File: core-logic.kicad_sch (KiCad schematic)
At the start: 32 parts, among them J5 TC2030-IDC, SW1 SW_Push, U1 STM32H723ZGI6, Y1 NX3215SA 32.768kHz, Y2 NX2016SA 25MHz

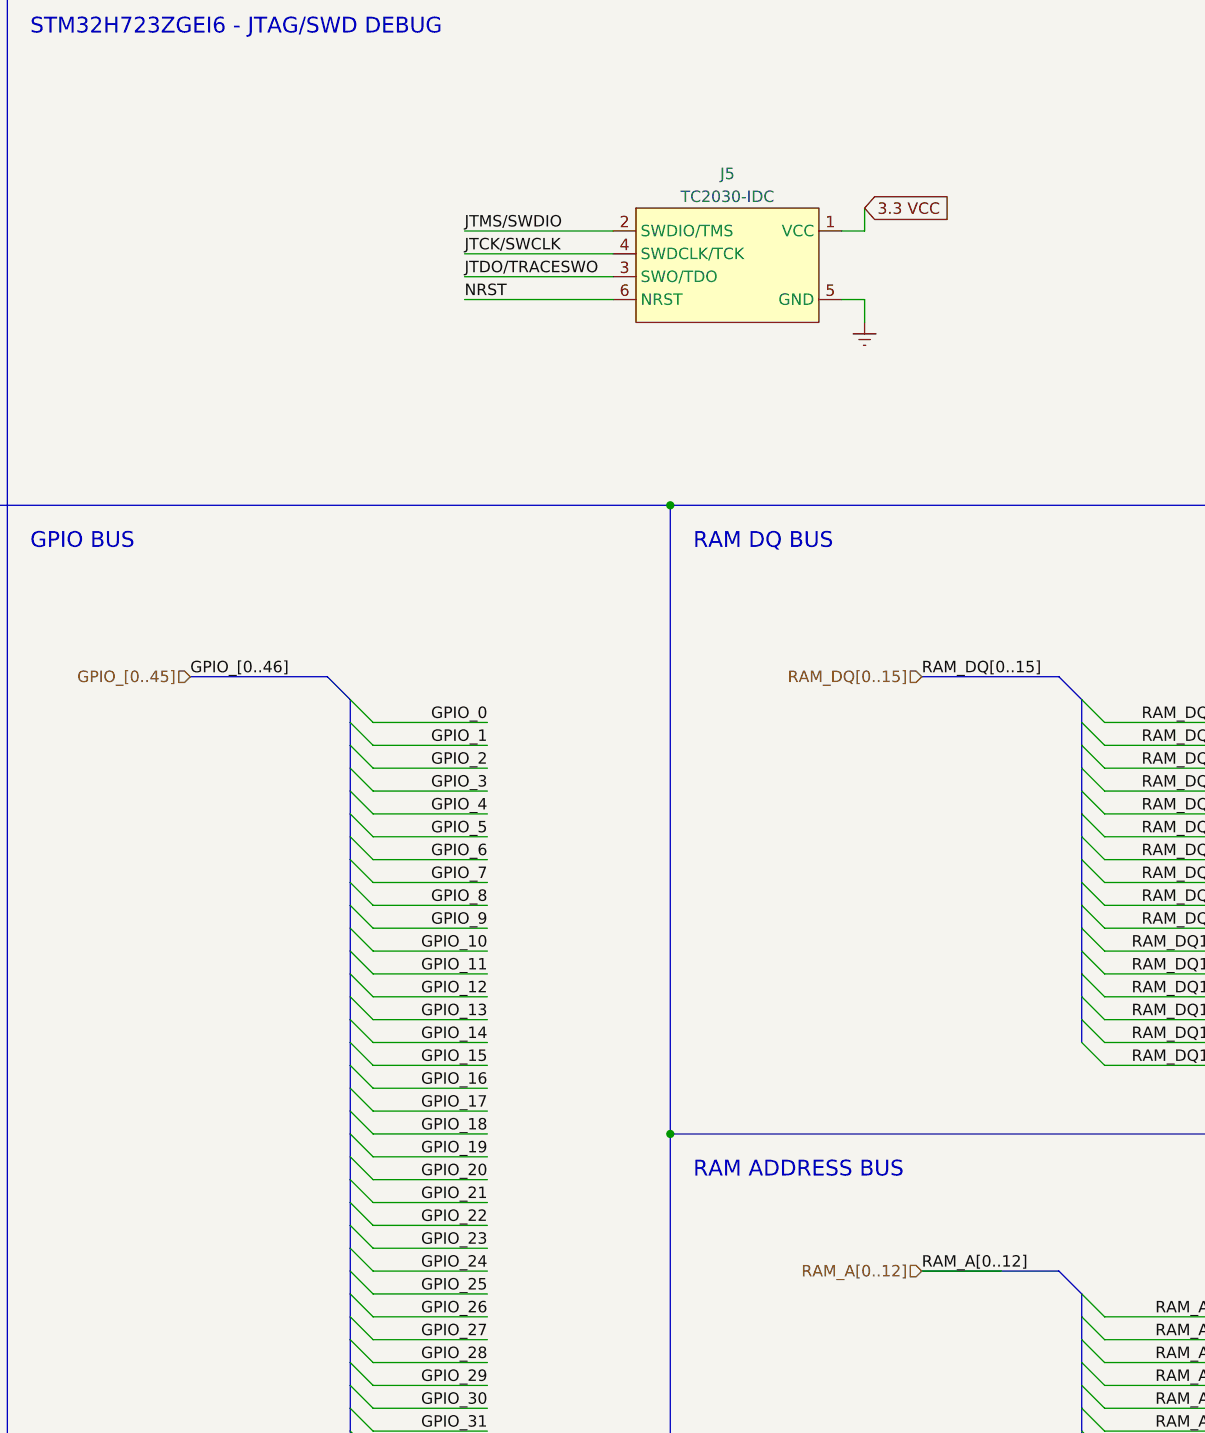
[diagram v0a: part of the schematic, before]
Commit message: updated bus aliases; added resistor values to RF section; added component to Fruitly_RF library
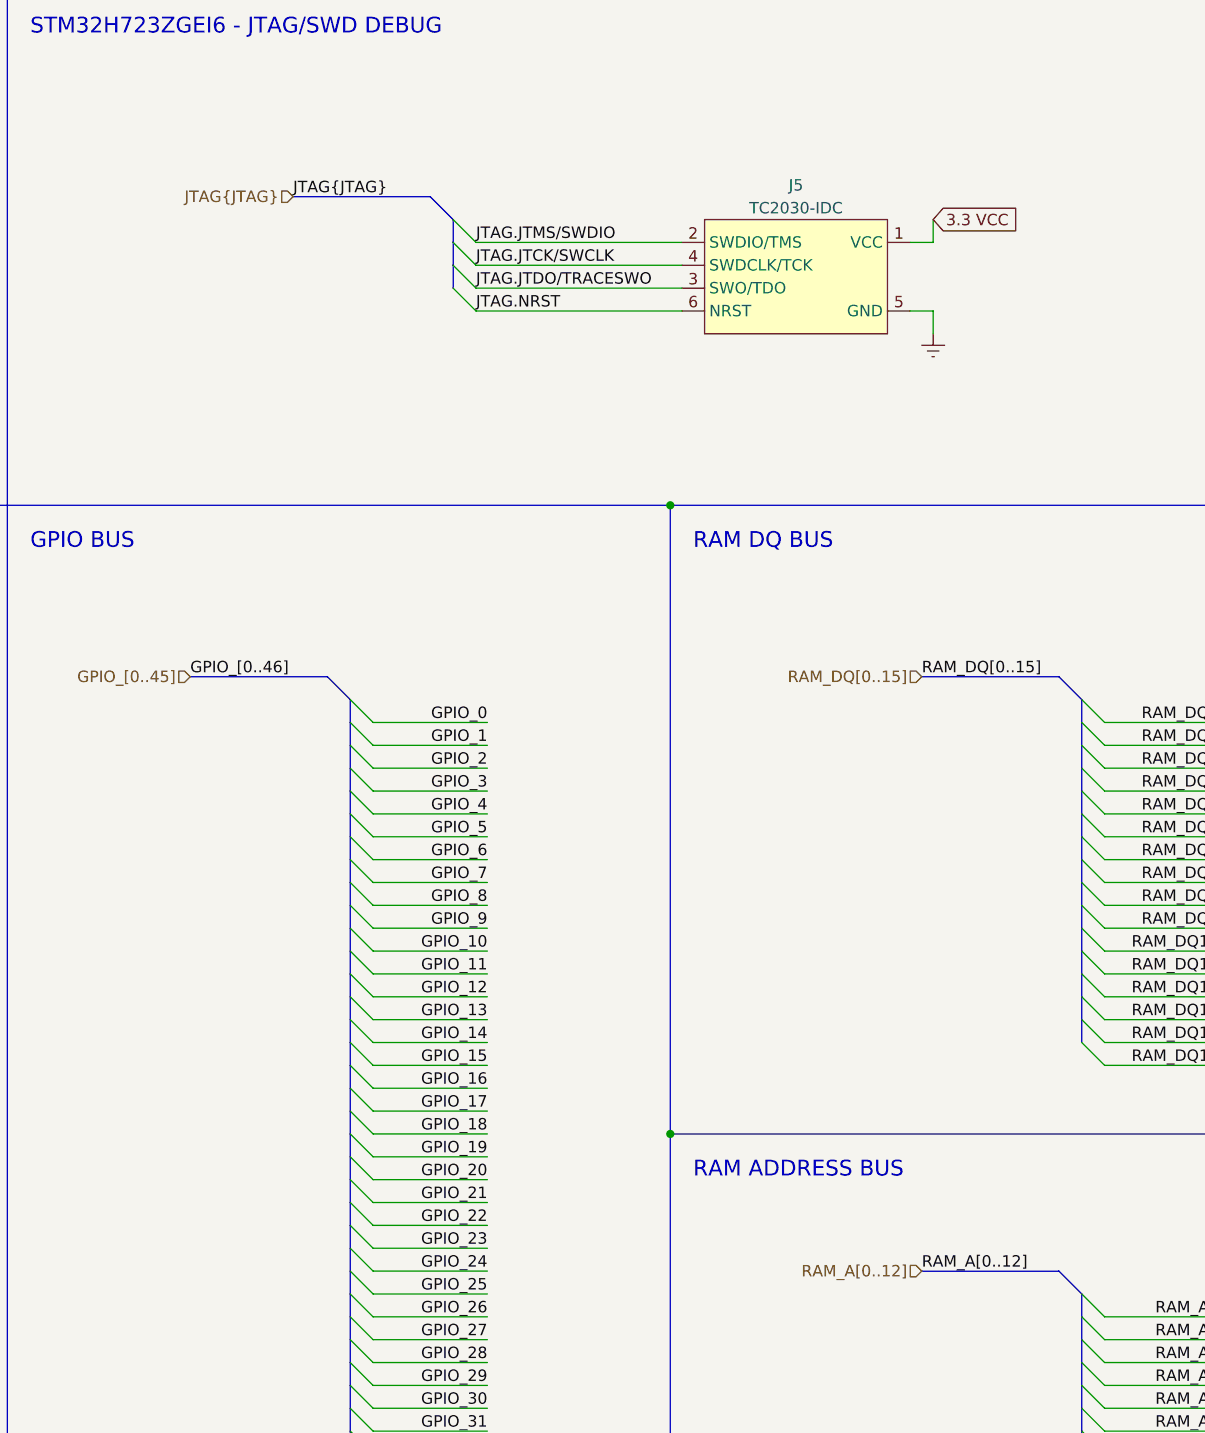
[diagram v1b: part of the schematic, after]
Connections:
- net JTCK/SWCLK: no longer J5.4 (SWDCLK/TCK)
- net JTDO/TRACESWO: no longer J5.3 (SWO/TDO)
- net JTMS/SWDIO: no longer J5.2 (SWDIO/TMS)
- net NRST: no longer J5.6 (NRST)
- new net JTAG.JTCK/SWCLK: J5.4 (SWDCLK/TCK)
- new net JTAG.JTDO/TRACESWO: J5.3 (SWO/TDO)
- new net JTAG.JTMS/SWDIO: J5.2 (SWDIO/TMS)
- new net JTAG.NRST: J5.6 (NRST)
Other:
- moved on the sheet: J5
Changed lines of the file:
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@@
     (company "Cerebral Systems Inc.")
   )
+  (bus_alias "JTAG" (members "JTMS/SWDIO" "JTCK/SWCLK" "JTDO/TRACESWO" "NRST"))
   (junction (at 113.03 232.41) (diameter 0) (color 0 0 0 0)
   )
@@
     (stroke (width 0) (type default) (color 255 153 0 1))
   )
+  (bus_entry (at 339.09 41.91) (size 2.54 2.54)
+    (stroke (width 0) (type default) (color 0 0 0 0))
+  )
   (bus_entry (at 407.67 227.33) (size 2.54 2.54)
     (stroke (width 0) (type default) (color 0 0 0 0))
@@
     (stroke (width 0) (type default) (color 255 153 0 1))
   )
+  (bus_entry (at 339.09 44.45) (size 2.54 2.54)
+    (stroke (width 0) (type default) (color 0 0 0 0))
+  )
   (bus_entry (at 408.94 189.23) (size 2.54 2.54)
     (stroke (width 0) (type default) (color 0 255 255 1))
@@
     (stroke (width 0) (type default) (color 255 153 0 1))
   )
+  (bus_entry (at 339.09 46.99) (size 2.54 2.54)
+    (stroke (width 0) (type default) (color 0 0 0 0))
+  )
   (bus_entry (at 327.66 156.21) (size 2.54 2.54)
     (stroke (width 0) (type default) (color 255 153 0 1))
@@
     (stroke (width 0) (type default) (color 0 0 0 0))
   )
+  (bus_entry (at 339.09 39.37) (size 2.54 2.54)
+    (stroke (width 0) (type default) (color 0 0 0 0))
+  )
   (bus_entry (at 327.66 143.51) (size 2.54 2.54)
     (stroke (width 0) (type default) (color 255 153 0 1))
@@
     (stroke (width 0) (type default) (color 0 0 0 0))
   )
-  (wire (pts (xy 356.87 43.18) (xy 340.36 43.18))
-    (stroke (width 0) (type default) (color 0 0 0 0))
-  )
   (bus (pts (xy 289.56 194.31) (xy 13.97 194.31))
     (stroke (width 0) (type dash) (color 0 0 0 0))
@@
     (stroke (width 0) (type default) (color 255 153 0 1))
   )
-  (wire (pts (xy 340.36 45.72) (xy 356.87 45.72))
-    (stroke (width 0) (type default) (color 0 0 0 0))
-  )
   (wire (pts (xy 196.85 180.34) (xy 171.45 180.34))
     (stroke (width 0) (type default) (color 0 255 255 1))
@@
     (stroke (width 0) (type default) (color 0 0 0 0))
   )
-  (wire (pts (xy 391.16 156.21) (xy 400.05 156.21))
-    (stroke (width 0) (type default) (color 0 0 0 0))
-  )
   (bus (pts (xy 327.66 135.89) (xy 327.66 138.43))
     (stroke (width 0) (type default) (color 0 0 0 0))
@@
     (stroke (width 0) (type dash) (color 0 0 0 0))
   )
-  (wire (pts (xy 384.81 38.1) (xy 384.81 40.64))
+  (wire (pts (xy 392.43 39.37) (xy 392.43 41.91))
     (stroke (width 0) (type default) (color 0 0 0 0))
   )
@@
     (stroke (width 0) (type default) (color 194 0 194 1))
   )
-  (wire (pts (xy 340.36 48.26) (xy 356.87 48.26))
-    (stroke (width 0) (type default) (color 0 0 0 0))
-  )
   (wire (pts (xy 137.16 262.89) (xy 137.16 264.16))
     (stroke (width 0) (type default) (color 0 0 0 0))
@@
     (stroke (width 0) (type default) (color 0 0 0 0))
   )
-  (wire (pts (xy 340.36 40.64) (xy 356.87 40.64))
-    (stroke (width 0) (type default) (color 0 0 0 0))
-  )
   (wire (pts (xy 410.21 227.33) (xy 436.88 227.33))
     (stroke (width 0) (type default) (color 0 0 0 0))
@@
     (stroke (width 0) (type default) (color 0 0 0 0))
   )
-  (wire (pts (xy 382.27 48.26) (xy 384.81 48.26))
+  (wire (pts (xy 389.89 49.53) (xy 392.43 49.53))
     (stroke (width 0) (type default) (color 0 0 0 0))
   )
@@
     (stroke (width 0) (type default) (color 194 0 194 1))
   )
+  (bus (pts (xy 321.31 36.83) (xy 336.55 36.83))
+    (stroke (width 0) (type default) (color 0 0 0 0))
+  )
   (wire (pts (xy 411.48 171.45) (xy 424.18 171.45))
     (stroke (width 0) (type default) (color 0 255 255 1))
@@
     (stroke (width 0) (type default) (color 0 0 0 0))
   )
-  (wire (pts (xy 382.27 40.64) (xy 384.81 40.64))
+  (wire (pts (xy 389.89 41.91) (xy 392.43 41.91))
     (stroke (width 0) (type default) (color 0 0 0 0))
   )
@@
     (stroke (width 0) (type default) (color 0 0 0 0))
   )
+  (bus (pts (xy 339.09 46.99) (xy 339.09 44.45))
+    (stroke (width 0) (type default) (color 0 0 0 0))
+  )
   (wire (pts (xy 411.48 120.65) (xy 424.18 120.65))
     (stroke (width 0) (type default) (color 194 0 194 1))
@@
     (stroke (width 0) (type default) (color 0 0 0 0))
   )
+  (wire (pts (xy 341.63 46.99) (xy 364.49 46.99))
+    (stroke (width 0) (type default) (color 0 0 0 0))
+  )
   (wire (pts (xy 62.23 55.88) (xy 62.23 48.26))
     (stroke (width 0) (type default) (color 0 0 0 0))
@@
     (stroke (width 0) (type default) (color 255 153 0 1))
   )
+  (bus (pts (xy 339.09 39.37) (xy 339.09 41.91))
+    (stroke (width 0) (type default) (color 0 0 0 0))
+  )
   (wire (pts (xy 411.48 186.69) (xy 424.18 186.69))
     (stroke (width 0) (type default) (color 0 255 255 1))
@@
     (stroke (width 0) (type default) (color 0 0 0 0))
   )
+  (wire (pts (xy 341.63 44.45) (xy 364.49 44.45))
+    (stroke (width 0) (type default) (color 0 0 0 0))
+  )
   (wire (pts (xy 124.46 262.89) (xy 124.46 256.54))
     (stroke (width 0) (type default) (color 0 0 0 0))
@@
     (stroke (width 0) (type default) (color 0 0 0 0))
   )
+  (wire (pts (xy 341.63 49.53) (xy 364.49 49.53))
+    (stroke (width 0) (type default) (color 0 0 0 0))
+  )
   (wire (pts (xy 104.14 259.08) (xy 111.76 259.08))
     (stroke (width 0) (type default) (color 0 0 0 0))
@@
     (stroke (width 0) (type default) (color 255 153 0 1))
   )
+  (bus (pts (xy 339.09 39.37) (xy 336.55 36.83))
+    (stroke (width 0) (type default) (color 0 0 0 0))
+  )
   (wire (pts (xy 196.85 175.26) (xy 171.45 175.26))
     (stroke (width 0) (type default) (color 0 255 255 1))
@@
     (stroke (width 0) (type default) (color 255 153 0 1))
   )
-  (wire (pts (xy 384.81 48.26) (xy 384.81 50.8))
+  (wire (pts (xy 392.43 49.53) (xy 392.43 52.07))
     (stroke (width 0) (type default) (color 0 0 0 0))
   )
@@
     (stroke (width 0) (type default) (color 255 153 0 1))
   )
+  (bus (pts (xy 339.09 44.45) (xy 339.09 41.91))
+    (stroke (width 0) (type default) (color 0 0 0 0))
+  )
   (wire (pts (xy 196.85 147.32) (xy 171.45 147.32))
     (stroke (width 0) (type default) (color 0 255 255 1))
@@
     (stroke (width 0) (type default) (color 0 0 0 0))
   )
+  (wire (pts (xy 341.63 41.91) (xy 364.49 41.91))
+    (stroke (width 0) (type default) (color 0 0 0 0))
+  )
   (bus (pts (xy 13.97 13.97) (xy 13.97 71.12))
     (stroke (width 0) (type dash) (color 0 0 0 0))
@@
     (effects (font (size 1.27 1.27)) (justify right bottom))
   )
-  (label "JTDO{slash}TRACESWO" (at 340.36 45.72 0)
+  (label "JTAG.JTDO{slash}TRACESWO" (at 341.63 46.99 0)
     (effects (font (size 1.27 1.27)) (justify left bottom))
   )
@@
     (effects (font (size 1.27 1.27)) (justify right bottom))
   )
-  (label "JTCK{slash}SWCLK" (at 340.36 43.18 0)
+  (label "JTAG.JTCK{slash}SWCLK" (at 341.63 44.45 0)
     (effects (font (size 1.27 1.27)) (justify left bottom))
   )
@@
     (effects (font (size 1.27 1.27)) (justify left bottom))
   )
-  (label "JTMS{slash}SWDIO" (at 340.36 40.64 0)
+  (label "JTAG.JTMS{slash}SWDIO" (at 341.63 41.91 0)
     (effects (font (size 1.27 1.27)) (justify left bottom))
   )
@@
     (effects (font (size 1.27 1.27)) (justify right bottom))
   )
+  (label "JTAG{JTAG}" (at 321.31 36.83 0)
+    (effects (font (size 1.27 1.27)) (justify left bottom))
+  )
   (label "RAM_A2" (at 424.18 166.37 180)
     (effects (font (size 1.27 1.27)) (justify right bottom))
@@
     (effects (font (size 1.27 1.27)) (justify right bottom))
   )
-  (label "NRST" (at 340.36 48.26 0)
+  (label "JTAG.NRST" (at 341.63 49.53 0)
     (effects (font (size 1.27 1.27)) (justify left bottom))
   )
@@
     (effects (font (size 1.27 1.27)) (justify right bottom))
   )
-  (global_label "3.3 VCC" (shape input) (at 384.81 38.1 0) (fields_autoplaced)
+  (global_label "3.3 VCC" (shape input) (at 392.43 39.37 0) (fields_autoplaced)
     (effects (font (size 1.27 1.27)) (justify left))
-    (property "Intersheet References" "${INTERSHEET_REFS}" (id 0) (at 394.8431 38.0206 0)
+    (property "Intersheet References" "${INTERSHEET_REFS}" (id 0) (at 402.4631 39.2906 0)
       (effects (font (size 1.27 1.27)) (justify left) hide)
     )
@@
     (effects (font (size 1.27 1.27)) (justify left))
   )
+  (hierarchical_label "JTAG{JTAG}" (shape input) (at 321.31 36.83 180)
+    (effects (font (size 1.27 1.27)) (justify right))
+  )
   (hierarchical_label "RAM_A[0..12]" (shape input) (at 391.16 156.21 180)
     (effects (font (size 1.27 1.27)) (justify right))
@@
     (pin "1")
   )
-  (symbol (lib_id "Connector:TC2030-IDC") (at 369.57 38.1 0) (unit 1)
+  (symbol (lib_id "Connector:TC2030-IDC") (at 377.19 39.37 0) (unit 1)
     (in_bom yes) (on_board yes) (fields_autoplaced)
-    (property "Reference" "J5" (id 0) (at 369.57 34.29 0))
-    (property "Value" "TC2030-IDC" (id 1) (at 369.57 36.83 0))
-    (property "Footprint" "" (id 2) (at 358.14 33.02 0)
+    (property "Reference" "J5" (id 0) (at 377.19 35.56 0))
+    (property "Value" "TC2030-IDC" (id 1) (at 377.19 38.1 0))
+    (property "Footprint" "" (id 2) (at 365.76 34.29 0)
       (effects (font (size 1.27 1.27)) hide)
     )
-    (property "Datasheet" "" (id 3) (at 358.14 33.02 0)
+    (property "Datasheet" "" (id 3) (at 365.76 34.29 0)
       (effects (font (size 1.27 1.27)) hide)
     )
@@
     (pin "1")
   )
-  (symbol (lib_id "power:Earth") (at 384.81 50.8 0) (unit 1)
+  (symbol (lib_id "power:Earth") (at 392.43 52.07 0) (unit 1)
     (in_bom yes) (on_board yes) (fields_autoplaced)
-    (property "Reference" "#PWR0117" (id 0) (at 384.81 57.15 0)
+    (property "Reference" "#PWR0117" (id 0) (at 392.43 58.42 0)
       (effects (font (size 1.27 1.27)) hide)
     )
-    (property "Value" "Earth" (id 1) (at 384.81 54.61 0)
+    (property "Value" "Earth" (id 1) (at 392.43 55.88 0)
       (effects (font (size 1.27 1.27)) hide)
     )
-    (property "Footprint" "" (id 2) (at 384.81 50.8 0)
+    (property "Footprint" "" (id 2) (at 392.43 52.07 0)
       (effects (font (size 1.27 1.27)) hide)
     )
-    (property "Datasheet" "~" (id 3) (at 384.81 50.8 0)
+    (property "Datasheet" "~" (id 3) (at 392.43 52.07 0)
       (effects (font (size 1.27 1.27)) hide)
     )
